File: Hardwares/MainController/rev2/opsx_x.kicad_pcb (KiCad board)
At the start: 2 copper layers, 95.9 x 27.8 mm, 61 parts, among them J1 Conn_01x02, J3 Conn_01x02, Q1 Q_NMOS_GSD, Q2 Q_NMOS_GSD, Q3 Q_PMOS_GSD, Q4 MMBT3904, U1 RP2040, U2 TLV70433DBVR, U3 W25Q128JVS, U4 OPTICAL-TSL2561T(6P-3.8X2.6MM), Y1 Crystal_GND2

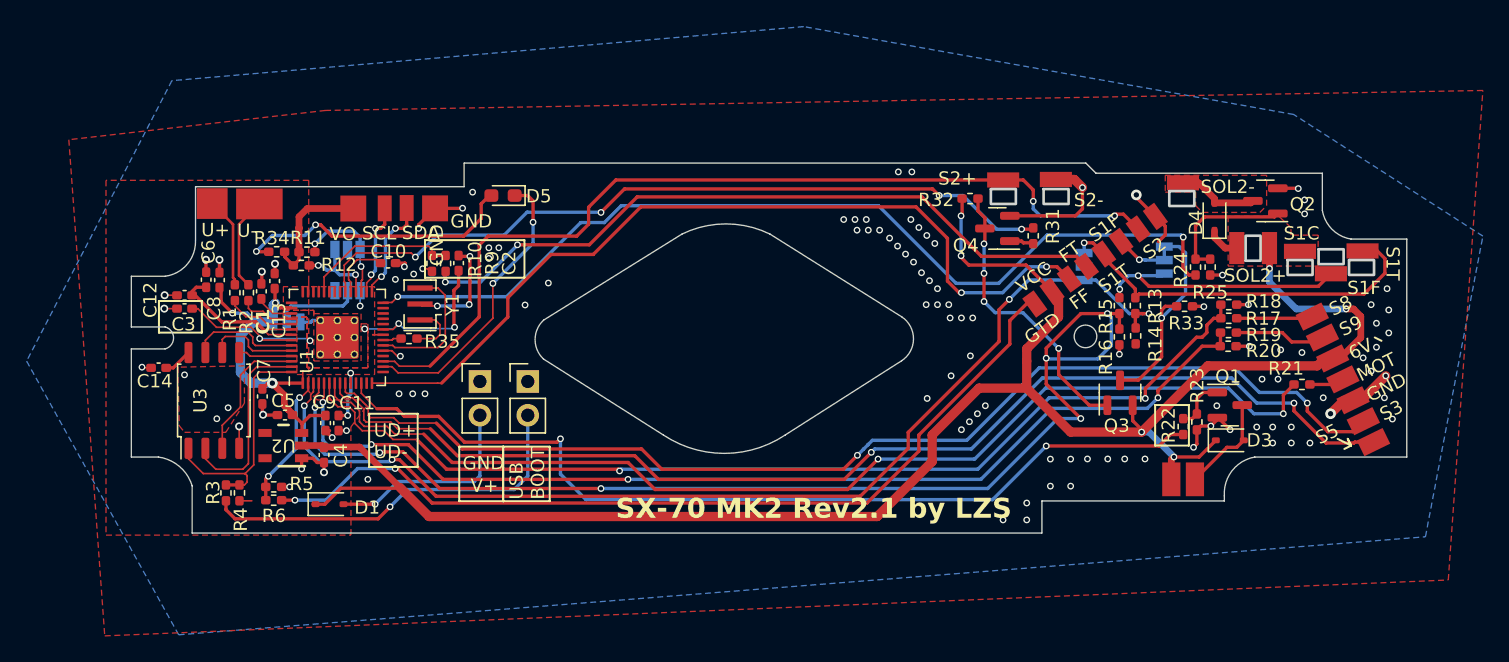
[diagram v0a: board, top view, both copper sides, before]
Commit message: 硬件更新：新增 Rev3_Normal 主板设计、FPC 柔性电路板、PowerBack 导光片壳体
- 新增 MainController Rev3_Normal (SX70z_Normal KiCad 工程 + Gerber + BOM)
- 新增 Fabrication BodyFPC 柔性电路板 Gerber
- 更新 MainController rev2 PCB
- 更新 PowerBack 外壳/快装板/导光片 (SLDPRT + STL + 3MF)

Co-Authored-By: Claude Opus 4.7 <noreply@anthropic.com>
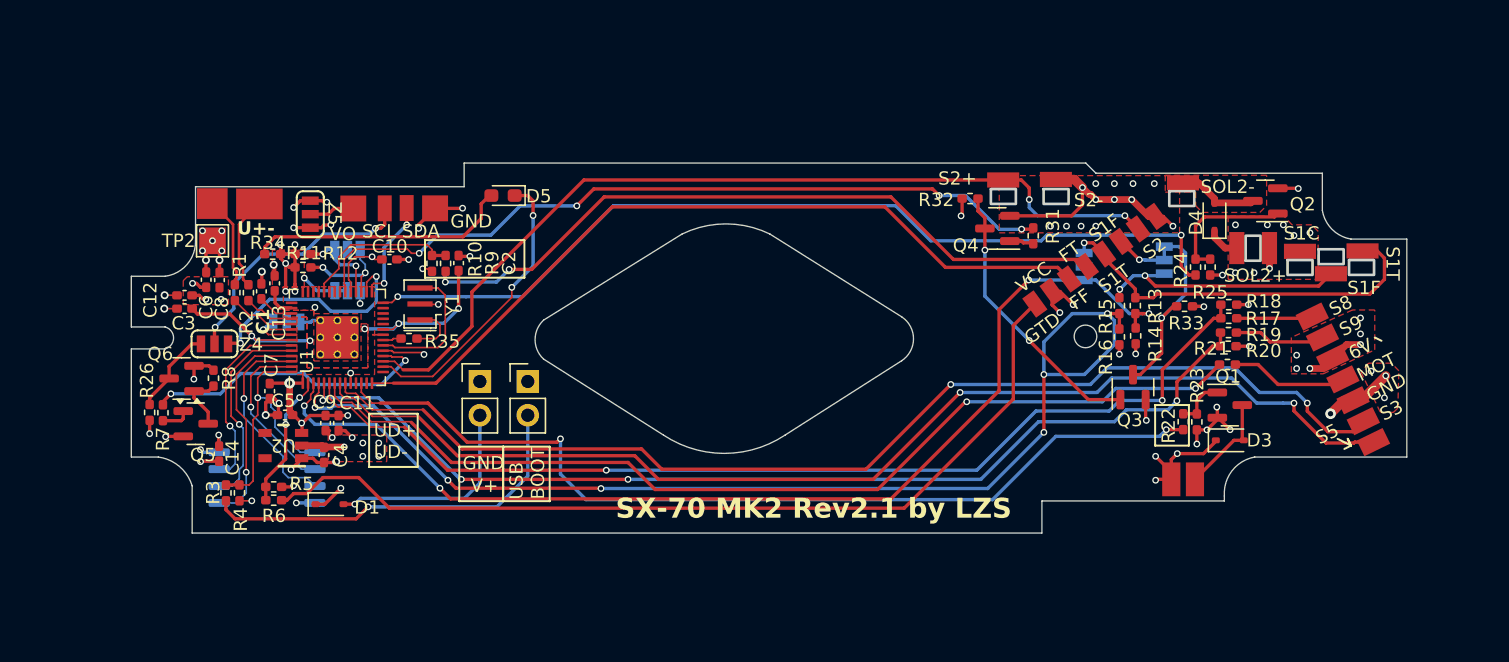
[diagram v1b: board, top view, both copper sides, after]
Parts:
- added Q5: MMBT3904, Package_TO_SOT_SMD:SOT-23, F.Cu at (30.2, 77.3)
- added Q6: Q_PMOS_GSD, Package_TO_SOT_SMD:SOT-23, F.Cu at (29.2, 73.9)
- added R26: 2.7k, Resistor_SMD:R_0402_1005Metric_Pad0.72x0.64mm_HandSolder, F.Cu at (26.8, 76.5)
- added R7: 5.6k, Resistor_SMD:R_0402_1005Metric_Pad0.72x0.64mm_HandSolder, F.Cu at (27.8, 76.5)
- added R8: 47k, Resistor_SMD:R_0402_1005Metric_Pad0.72x0.64mm_HandSolder, F.Cu at (31.6, 73.9)
- added TP2: TestPoint, TestPoint:TestPoint_Pad_2.0x2.0mm, F.Cu at (31.5, 63.6)
- added Z4: ~, OPSX:Selector_default, F.Cu at (31.6, 71.4)
- added Z5: ~, OPSX:Selector_default, F.Cu at (38.8, 61.5)
- U3: moved to B.Cu
- moved C14 7.89 mm to (32.0, 79.6), turned to -90 degrees
- moved U3 7.05 mm to (35.6, 81.4), turned to 180 degrees
- moved R21 5.80 mm to (107.8, 72.9)
- moved R11 1.19 mm to (38.3, 65.6)
- moved Q3 1.06 mm to (100.7, 74.6)
- moved R12 0.86 mm to (38.3, 64.6)
- moved C7 0.68 mm to (35.8, 74.9)
- moved R22 0.37 mm to (104.5, 77.2)
- moved R34 0.35 mm to (36.0, 64.6)
- moved C10 0.29 mm to (44.8, 65.0)
- moved C13 0.17 mm to (36.2, 66.8)
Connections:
- U1 pad 18: unconnected-(U1-GPIO15-Pad18) -> /FF_Left_MCU
- sx1 pad SCL: /SCL1 -> /FF_Left_Board
- sx1 pad VO: +3.3V -> /VO_Left_Board
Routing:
- net VCC: track 144.8 -> 108.2 mm, vias 6 -> 30
- net /FF_Left_MCU: track 0.00 -> 22.0 mm, vias 0 -> 2
- net /FF_Left_Board: track 0.00 -> 19.5 mm, vias 0 -> 2
- net +3.3V: track 63.6 -> 44.9 mm, vias 6 -> 21
- net /QSPI_SD0: track 4.06 -> 16.3 mm, vias 0 -> 1
- net /SCL1: track 7.06 -> 17.3 mm
- net /QSPI_SCLK: track 7.03 -> 15.5 mm, vias 0 -> 1
- net Net-(U1-GPIO5): track 82.2 -> 74.3 mm
- net /FF_Left: track 0.00 -> 6.57 mm
- net /QSPI_SD3: track 8.34 -> 14.4 mm, vias 0 -> 1
- net /MOTOR: track 2.64 -> 8.32 mm
- net GND: track 75.2 -> 80.5 mm, vias 117 -> 58
- net /QSPI_SD2: track 10.3 -> 15.4 mm, vias 0 -> 1
- net Net-(Q5-C): track 0.00 -> 4.51 mm
- net /FF: track 64.5 -> 60.2 mm, vias 2 -> 0
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- added copper zone on In1.Cu, net +3.3V
- added copper zone on In2.Cu, net GND
- added copper zone on In1.Cu, net VCC
- removed copper zone on B.Cu, net GND
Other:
- copper layers 2 -> 4
